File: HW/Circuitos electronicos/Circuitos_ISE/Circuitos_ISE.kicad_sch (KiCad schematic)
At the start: 36 parts, among them J1 Conn_01x02, U1 OP07, U2 ADA4099-2xRM, U3 LT1009xZ, U4 TL074, U5 OP07, U6 OP07, U7 INA128, U9 OP07

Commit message: circuit complete rework
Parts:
- removed C_filter3: C, symbol Device:C
- removed R14, R17, R18, R4, R5, R6, R7, R9: R_US, symbol Device:R_US
- removed R_Ref: R_Potentiometer_US, symbol Device:R_Potentiometer_US
- removed U1, U5, U6, U9: OP07, symbol Amplifier_Operational:OP07
- removed U2: ADA4099-2xRM, Package_SO:MSOP-8_3x3mm_P0.65mm, symbol Amplifier_Operational:ADA4099-2xRM
- removed U4: TL074, symbol Amplifier_Operational:TL074
- added C3: 33pF, symbol Device:C
- added C4: 47uF, symbol Device:C
- added C5, C6: C_Polarized, symbol Device:C_Polarized
- added U1: TL074, symbol Amplifier_Operational:TL074
- added U2: LM2596S-ADJ, Package_TO_SOT_SMD:TO-263-5_TabPin3, symbol Regulator_Switching:LM2596S-ADJ
- added U4: L7805, symbol Regulator_Linear:L7805
- C_filter2: value C -> 100n
- R10: renamed from R11; value R_US -> 10k
- R12: value R_US -> 150k
- R13, R16: value R_US -> 100k
- renumbered RG to 50k
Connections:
- net GND_A: now also 50k.1, R13.1, R16.1, C4.1, C5.1, C6.2, U4.3 (OUT)
- net Vcc: now also C6.1, U1.4 (V+), U2.2 (OUT), U4.1 (IN)
- net Vcc_meas: now also U2.1 (VIN)
- net Vee: now also C5.2, U1.11 (V-), U2.3 (GND), U4.2 (GND)
- net at C_filter2.2: now also R16.2, U1.3 (+)
- net at R10.2, R12.1: now also C3.1, U1.6 (-)
- net analog_out: now reaches R12.2
- net analog_out: now also C3.2, U1.7
- net at R13.2: now also 50k.2, U1.5 (+)
- net at R10.1: now also C4.2
- net at 50k.3: now also U1.1, U1.2 (-)
- no-connect marks 6 -> 2
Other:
- removed sheet Acondicionador de señal
- removed sheet Masa Virtual
- removed sheet Sensor de consumo
- moved on the sheet: 50k, C_filter2, R10, R12, R_Shunt

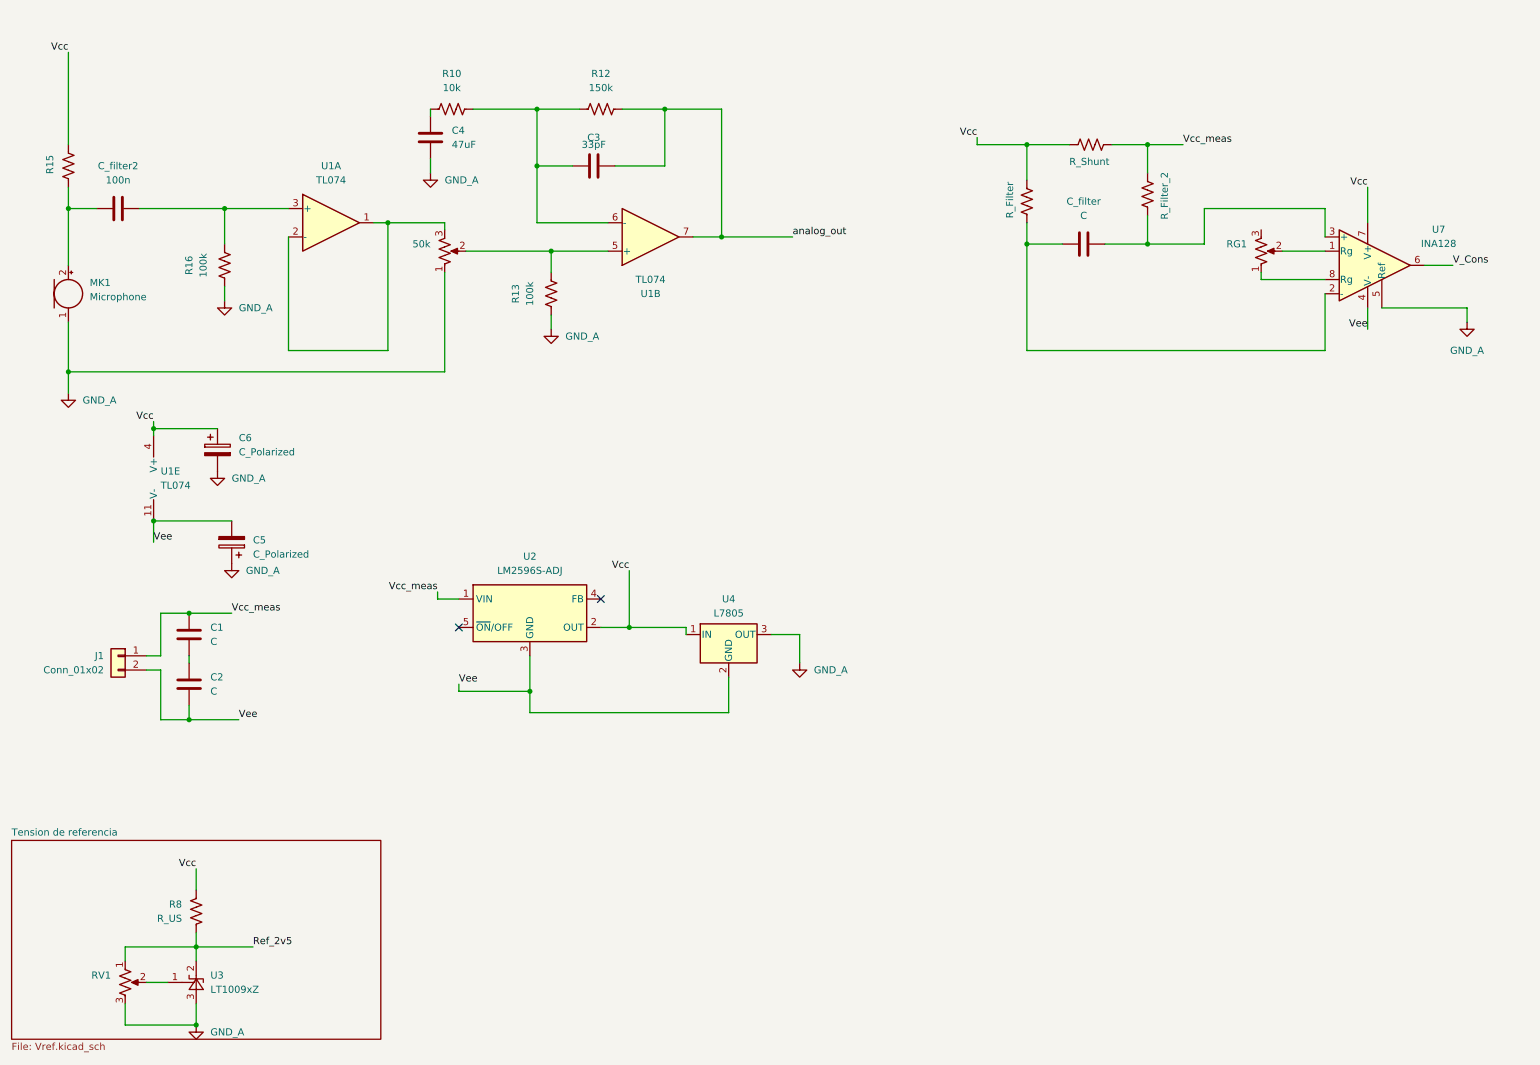
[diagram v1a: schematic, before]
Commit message: rework de alimentacion
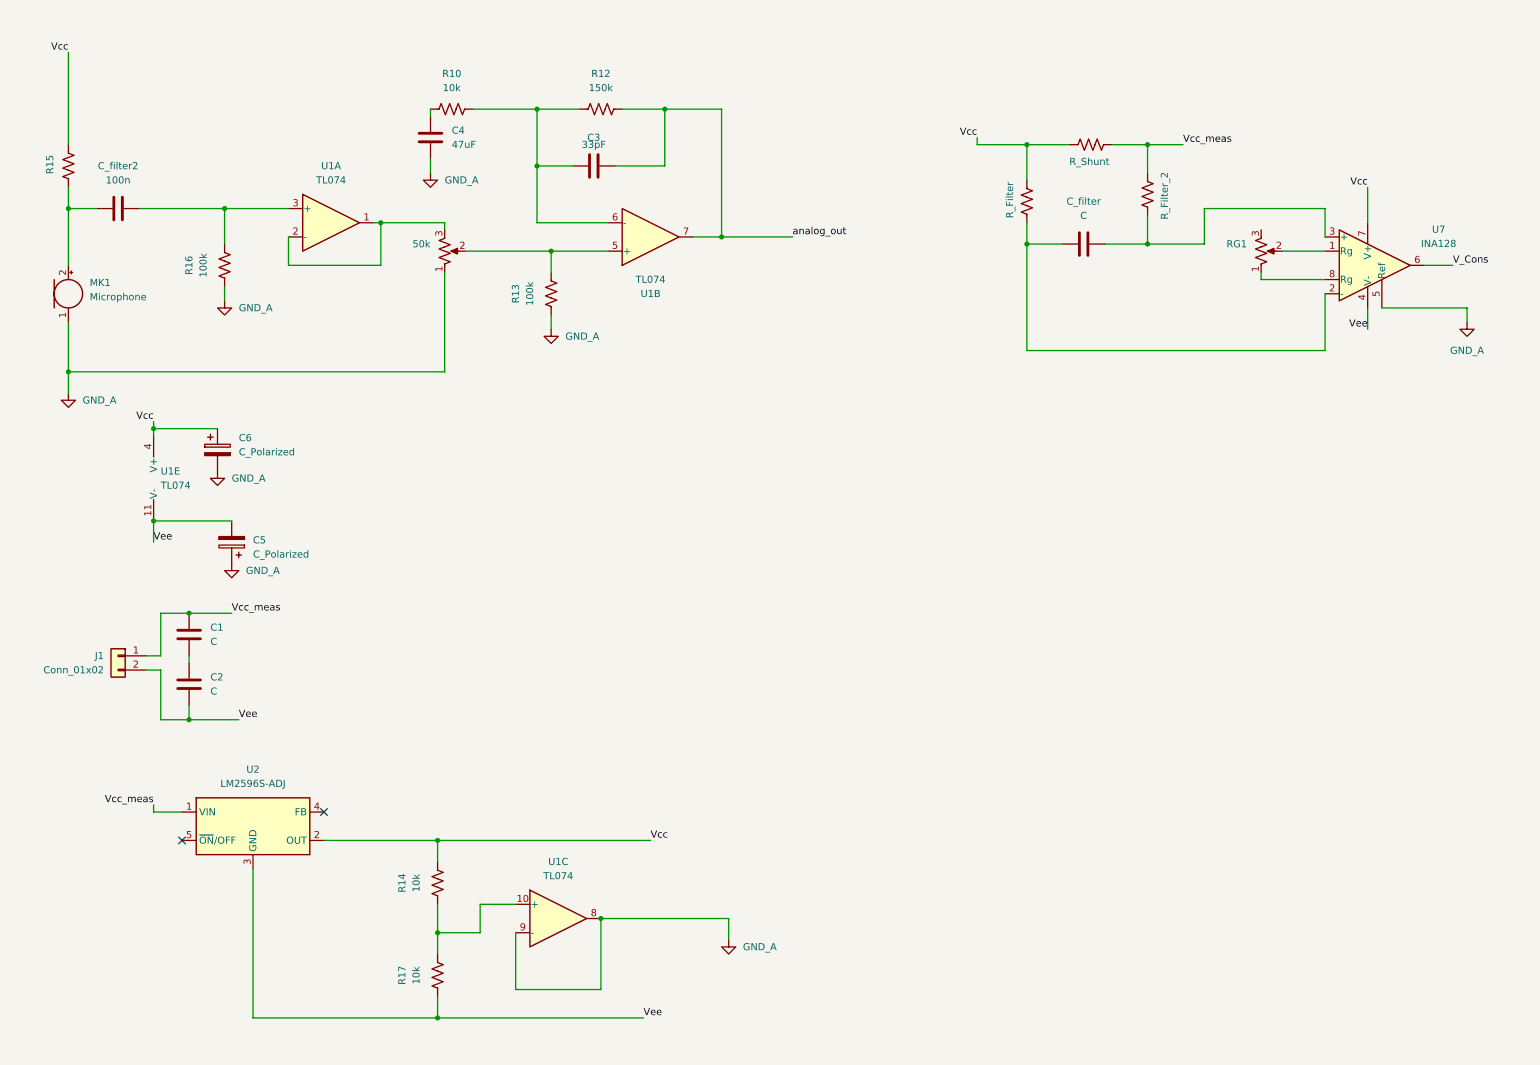
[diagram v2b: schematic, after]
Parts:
- removed R8: R_US, symbol Device:R_US
- removed RV1: R_Potentiometer_US, symbol Device:R_Potentiometer_US
- removed U3: LT1009xZ, Package_TO_SOT_THT:TO-92L_Inline, symbol Reference_Voltage:LT1009xZ
- removed U4: L7805, symbol Regulator_Linear:L7805
- added R14, R17: 10k, symbol Device:R_US
- added unit 3 of U1
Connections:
- net GND_A: now also U1.8, U1.9 (-)
- net Vcc: now also R14.2
- net Vee: now also R17.1
- new net: R14.1, R17.2, U1.10 (+)
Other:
- removed sheet Tension de referencia
- moved on the sheet: U2

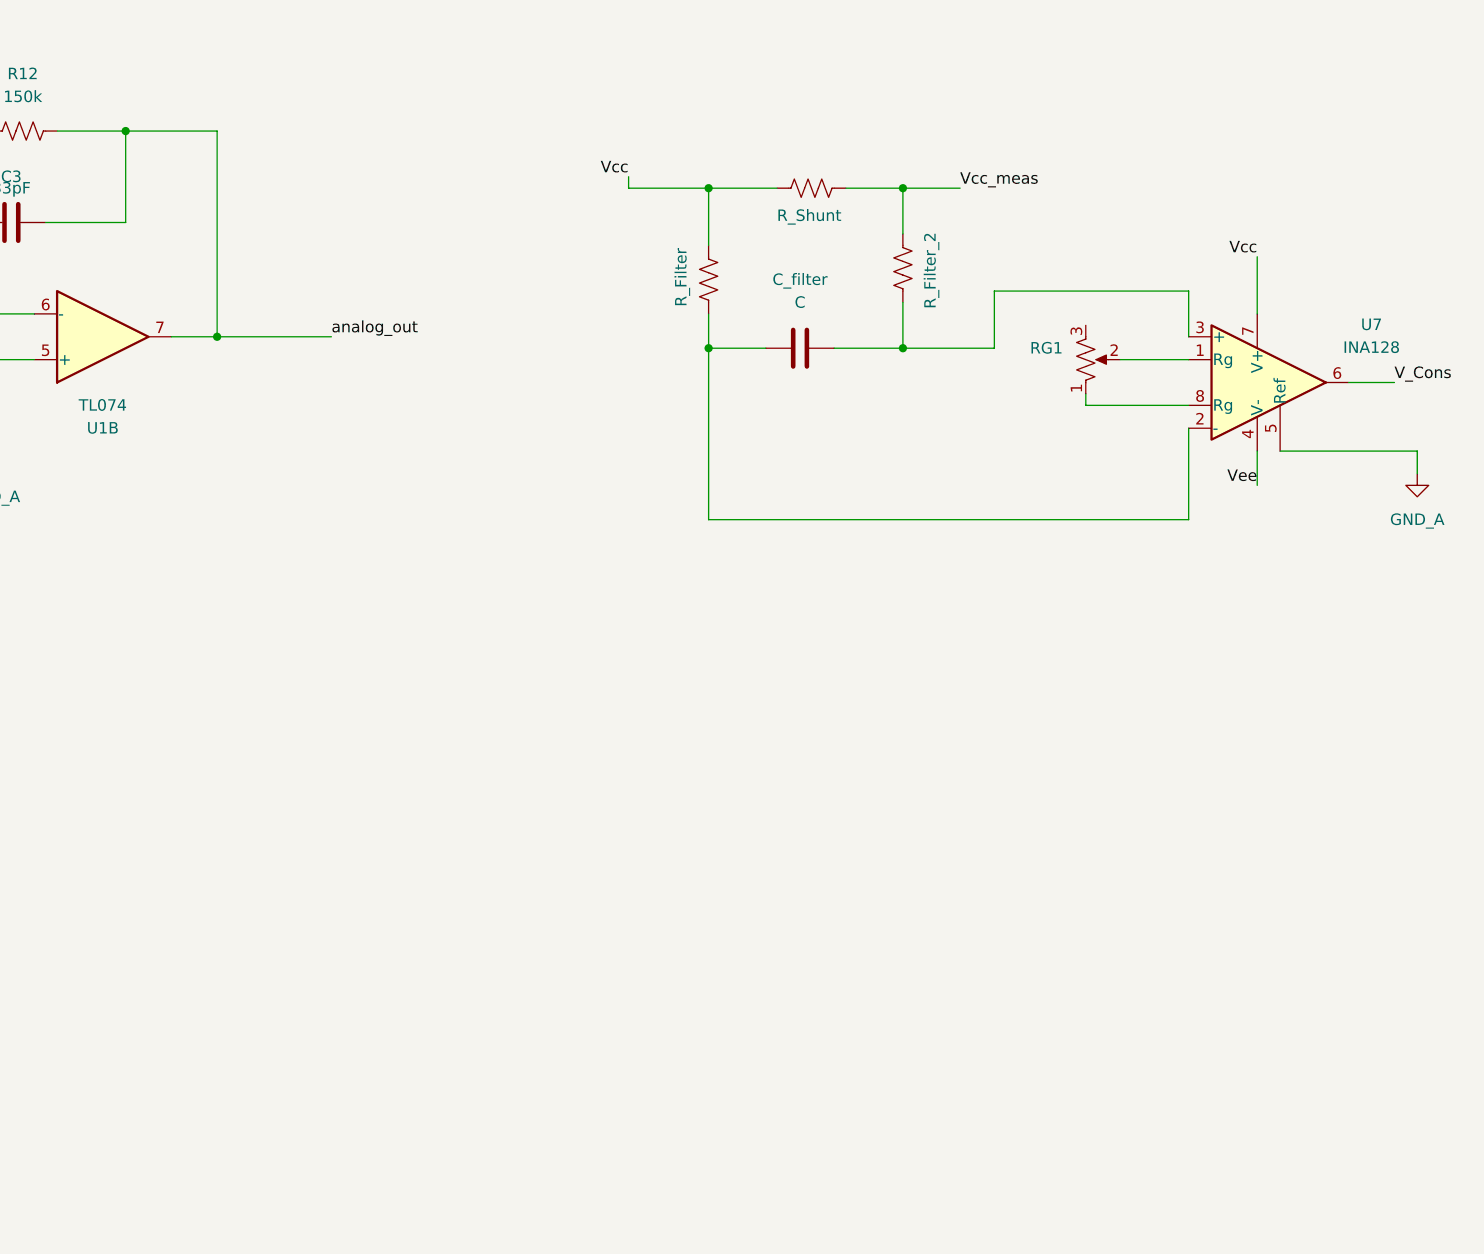
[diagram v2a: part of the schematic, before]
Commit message: Actualizacion de sensor de corriente
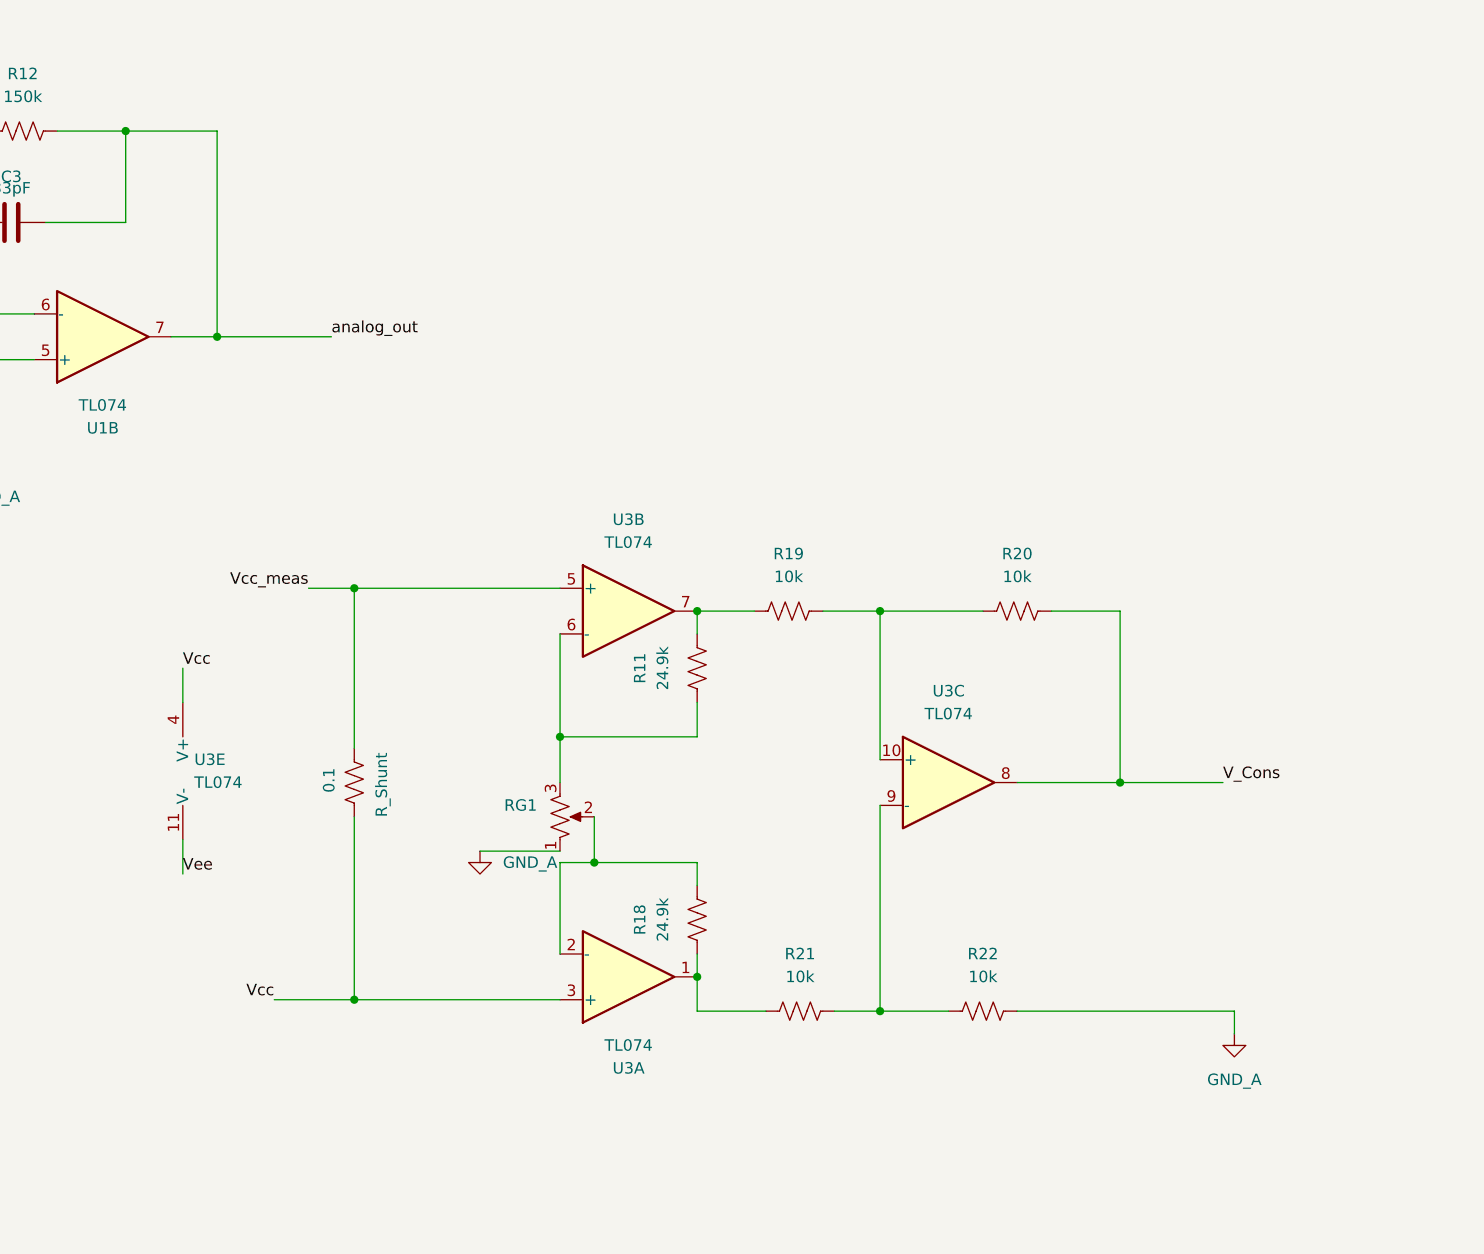
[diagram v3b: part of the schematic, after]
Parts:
- removed C_filter: C, symbol Device:C
- removed R_Filter, R_Filter_2: R_US, symbol Device:R_US
- removed U7: INA128, symbol Amplifier_Instrumentation:INA128
- added R11, R18: 24.9k, symbol Device:R_US
- added R19, R20, R21, R22: 10k, symbol Device:R_US
- added U3: TL074, symbol Amplifier_Operational:TL074
- R_Shunt: value R_US -> 0.1
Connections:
- net GND_A: now also RG1.1, R22.2
- net V_Cons: now also R20.2, U3.8
- net Vcc: now also U3.3 (+), U3.4 (V+)
- net Vcc_meas: now also U3.5 (+)
- net Vee: now also U3.11 (V-)
- net at RG1.2: now also R18.2, U3.2 (-)
- net at RG1.3: now also R11.1, U3.6 (-)
- new net: R11.2, R19.1, U3.7
- new net: R19.2, R20.1, U3.10 (+)
- new net: R18.1, R21.1, U3.1
- new net: R21.2, R22.1, U3.9 (-)
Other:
- moved on the sheet: RG1, R_Shunt

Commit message: Actualizacion de el circuito analogico
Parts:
- removed C1, C2: C, symbol Device:C
- added BT1, BT2: Battery_Cell, symbol Device:Battery_Cell
- added C7: C, symbol Device:C
- added D1: 1N4007, Diode_THT:D_DO-41_SOD81_P10.16mm_Horizontal, symbol Diode:1N4007
- added R23, R24, R25, R26, R28: 10k, symbol Device:R_US
- added R27: 150k, symbol Device:R_US
- added unit 3 of U1
- R10: value 10k -> 2.2k
- R12: value 150k -> 1M
- R13: value 100k -> 10k
- renumbered U3 to U2, U1 to U2
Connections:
- net GND_A: now also U2.13 (-), U2.14, C7.2, R24.1, R28.1; no longer U2.8, U2.9 (-)
- net Vcc: no longer C6.1, R14.2, R_Shunt.2, U1.4 (V+), U2.2 (OUT), U2.3 (+), U2.4 (V+)
- net at R19.2, R20.1: now also U2.9 (-); no longer U2.10 (+)
- net at R21.2, R22.1: now also U2.10 (+); no longer U2.9 (-)
- net at R14.1, R17.2: now also U2.12 (+); no longer U2.10 (+)
- net Vcc_meas: no longer names the net of R_Shunt.1, U2.5 (+)
- net Vcc_meas: now also BT1.2 (-); no longer J1.1 (Pin_1), U2.1 (VIN)
- net Vee renamed Vbat-
- net Vbat-: now also BT2.2 (-), R25.2
- net analog_out: no longer names the net of C3.2, R12.2, U1.7
- net analog_out: now also D1.2 (A)
- new net: BT2.1 (+), R_Shunt.2, U2.3 (+)
- new net: D1.1 (K), R27.1, R28.2
- new net: R23.2, R26.1, U1.9 (-)
- new net: R24.2, R25.1, U1.10 (+)
- new net: C7.1, R23.1, R27.2
- new net 10V: C6.1, R14.2, U1.4 (V+), U2.2 (OUT), U2.4 (V+)
- new net ANALOG_OUT: R26.2, U1.8
- new net Vbat+: BT1.1 (+), J1.1 (Pin_1), U2.1 (VIN)
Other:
- moved on the sheet: C5, C6, J1, R11, R14, R17, R18, R19, R20, R21, R22, RG1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
